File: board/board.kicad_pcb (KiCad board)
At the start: 2 copper layers, 102.4 x 54.4 mm, 20 parts, among them J1 FTDI_ISP, J2 ICSP, J3 Motor_Terminal, J4 Power, J5 Run, SW1 Run, SW2 Select, SW3 Up, SW4 Down, U1 ATmega328P-P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

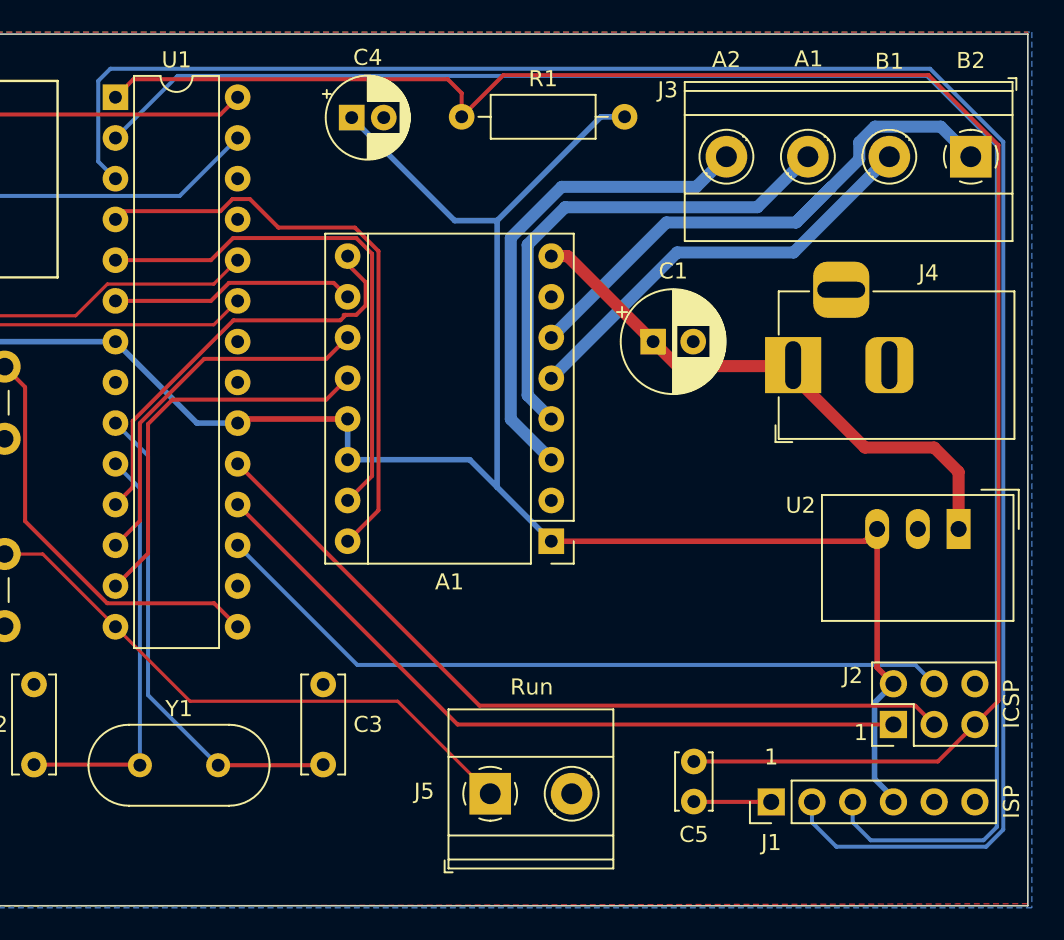
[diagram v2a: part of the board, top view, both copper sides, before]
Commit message: Fixed an overlapping trace that got missed in last DRC.
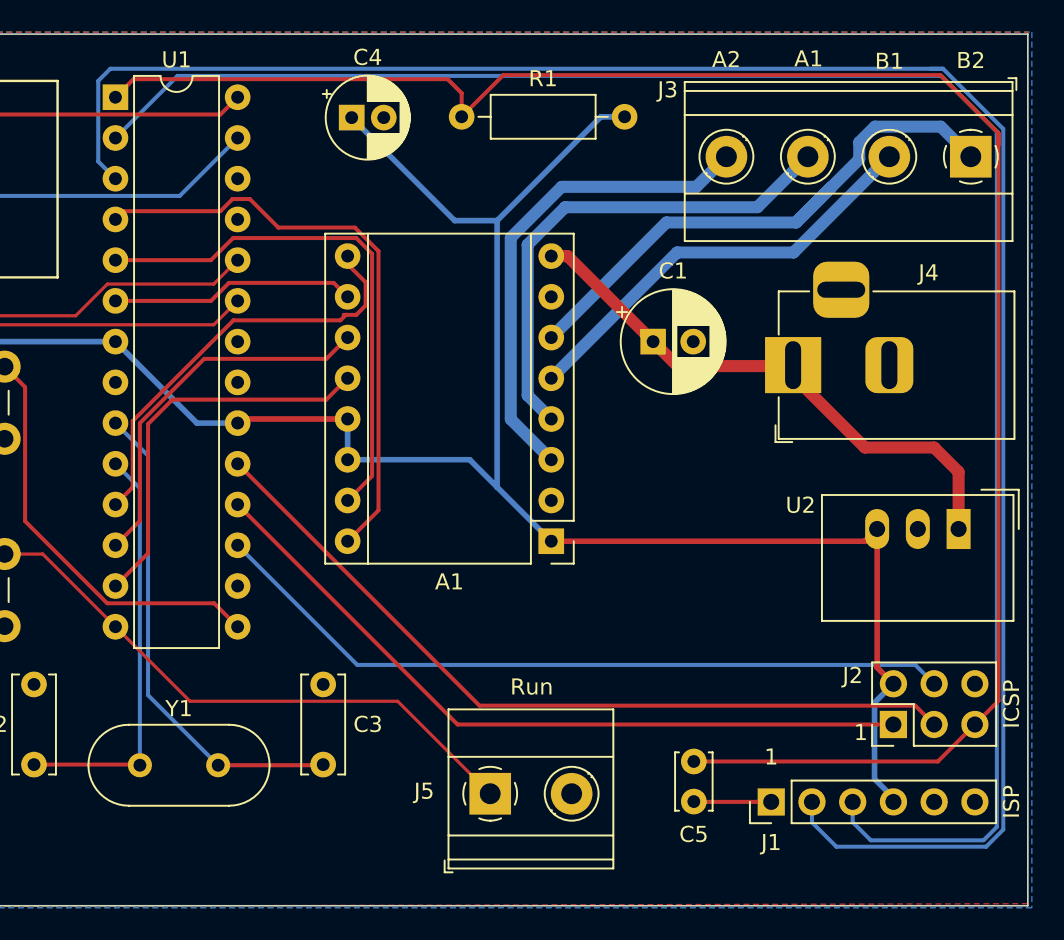
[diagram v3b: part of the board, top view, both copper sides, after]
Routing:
- net RX: track 111.9 -> 113.3 mm
- net TX: track 122.3 -> 123.6 mm
- net RESET: track 115.5 -> 116.6 mm
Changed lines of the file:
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@@
   (segment (start 175.514 72.336) (end 179.886 76.708) (width 0.25) (layer "B.Cu") (net 15))
   (segment (start 209.51 78.994) (end 214.376 78.994) (width 0.25) (layer "F.Cu") (net 16))
-  (segment (start 197.670211 33.672989) (end 195.072 36.2712) (width 0.25) (layer "F.Cu") (net 17))
-  (segment (start 224.186006 33.672989) (end 197.670211 33.672989) (width 0.25) (layer "F.Cu") (net 17))
-  (segment (start 227.076 74.168) (end 228.547011 72.696989) (width 0.25) (layer "F.Cu") (net 17))
+  (segment (start 224.919609 33.672989) (end 228.547011 37.300391) (width 0.25) (layer "F.Cu") (net 17))
+  (segment (start 228.547011 37.300391) (end 228.547011 38.033994) (width 0.25) (layer "F.Cu") (net 17))
+  (segment (start 195.072 36.2712) (end 197.670211 33.672989) (width 0.25) (layer "F.Cu") (net 17))
+  (segment (start 197.670211 33.672989) (end 224.919609 33.672989) (width 0.25) (layer "F.Cu") (net 17))
   (segment (start 194.200989 33.926989) (end 195.072 34.798) (width 0.25) (layer "F.Cu") (net 17))
+  (segment (start 228.547011 37.300391) (end 228.547011 72.696989) (width 0.25) (layer "F.Cu") (net 17))
+  (segment (start 228.547011 72.696989) (end 227.076 74.168) (width 0.25) (layer "F.Cu") (net 17))
   (segment (start 227.076 74.168) (end 224.77 76.474) (width 0.25) (layer "F.Cu") (net 17))
   (segment (start 195.072 34.798) (end 195.072 36.2712) (width 0.25) (layer "F.Cu") (net 17))
   (segment (start 224.77 76.474) (end 209.55 76.474) (width 0.25) (layer "F.Cu") (net 17))
   (segment (start 194.200989 33.926989) (end 174.607011 33.926989) (width 0.25) (layer "F.Cu") (net 17))
-  (segment (start 228.547011 72.696989) (end 228.547011 38.033994) (width 0.25) (layer "F.Cu") (net 17))
   (segment (start 174.607011 33.926989) (end 173.482 35.052) (width 0.25) (layer "F.Cu") (net 17))
-  (segment (start 228.547011 38.033994) (end 224.186006 33.672989) (width 0.25) (layer "F.Cu") (net 17))
-  (segment (start 228.447011 80.558006) (end 228.447011 38.081994) (width 0.25) (layer "B.Cu") (net 18))
-  (segment (start 220.581011 81.389011) (end 227.616006 81.389011) (width 0.25) (layer "B.Cu") (net 18))
-  (segment (start 177.351011 33.722989) (end 173.482 37.592) (width 0.25) (layer "B.Cu") (net 18))
-  (segment (start 219.456 78.994) (end 219.456 80.264) (width 0.25) (layer "B.Cu") (net 18))
-  (segment (start 228.447011 38.081994) (end 224.088006 33.722989) (width 0.25) (layer "B.Cu") (net 18))
-  (segment (start 227.616006 81.389011) (end 228.447011 80.558006) (width 0.25) (layer "B.Cu") (net 18))
-  (segment (start 224.088006 33.722989) (end 177.351011 33.722989) (width 0.25) (layer "B.Cu") (net 18))
-  (segment (start 219.456 80.264) (end 220.581011 81.389011) (width 0.25) (layer "B.Cu") (net 18))
-  (segment (start 228.847031 37.839031) (end 228.847031 80.7237) (width 0.25) (layer "B.Cu") (net 19))
-  (segment (start 227.7817 81.789031) (end 218.441031 81.789031) (width 0.25) (layer "B.Cu") (net 19))
-  (segment (start 218.441031 81.789031) (end 216.916 80.264) (width 0.25) (layer "B.Cu") (net 19))
-  (segment (start 172.406989 39.056989) (end 172.406989 34.031991) (width 0.25) (layer "B.Cu") (net 19))
-  (segment (start 173.16498 33.274) (end 224.282 33.274) (width 0.25) (layer "B.Cu") (net 19))
+  (segment (start 228.447011 37.200391) (end 228.447011 80.558006) (width 0.25) (layer "B.Cu") (net 18))
+  (segment (start 177.351011 33.722989) (end 224.969609 33.722989) (width 0.25) (layer "B.Cu") (net 18))
+  (segment (start 227.616006 81.389011) (end 220.581011 81.389011) (width 0.25) (layer "B.Cu") (net 18))
+  (segment (start 173.482 37.592) (end 177.351011 33.722989) (width 0.25) (layer "B.Cu") (net 18))
+  (segment (start 224.969609 33.722989) (end 228.447011 37.200391) (width 0.25) (layer "B.Cu") (net 18))
+  (segment (start 220.581011 81.389011) (end 219.456 80.264) (width 0.25) (layer "B.Cu") (net 18))
+  (segment (start 228.447011 37.200391) (end 228.447011 38.081994) (width 0.25) (layer "B.Cu") (net 18))
+  (segment (start 228.447011 80.558006) (end 227.616006 81.389011) (width 0.25) (layer "B.Cu") (net 18))
+  (segment (start 219.456 80.264) (end 219.456 78.994) (width 0.25) (layer "B.Cu") (net 18))
+  (segment (start 216.916 80.264) (end 218.441031 81.789031) (width 0.25) (layer "B.Cu") (net 19))
+  (segment (start 228.847031 80.7237) (end 228.847031 37.034697) (width 0.25) (layer "B.Cu") (net 19))
+  (segment (start 218.441031 81.789031) (end 227.7817 81.789031) (width 0.25) (layer "B.Cu") (net 19))
+  (segment (start 228.847031 37.034697) (end 225.086334 33.274) (width 0.25) (layer "B.Cu") (net 19))
   (segment (start 216.916 78.994) (end 216.916 80.264) (width 0.25) (layer "B.Cu") (net 19))
-  (segment (start 173.482 40.132) (end 172.406989 39.056989) (width 0.25) (layer "B.Cu") (net 19))
-  (segment (start 228.847031 80.7237) (end 227.7817 81.789031) (width 0.25) (layer "B.Cu") (net 19))
-  (segment (start 224.282 33.274) (end 228.847031 37.839031) (width 0.25) (layer "B.Cu") (net 19))
-  (segment (start 172.406989 34.031991) (end 173.16498 33.274) (width 0.25) (layer "B.Cu") (net 19))
+  (segment (start 172.406989 34.031991) (end 172.406989 39.056989) (width 0.25) (layer "B.Cu") (net 19))
+  (segment (start 225.086334 33.274) (end 173.16498 33.274) (width 0.25) (layer "B.Cu") (net 19))
+  (segment (start 172.406989 39.056989) (end 173.482 40.132) (width 0.25) (layer "B.Cu") (net 19))
+  (segment (start 227.7817 81.789031) (end 228.847031 80.7237) (width 0.25) (layer "B.Cu") (net 19))
+  (segment (start 225.086334 33.274) (end 224.282 33.274) (width 0.25) (layer "B.Cu") (net 19))
+  (segment (start 173.16498 33.274) (end 172.406989 34.031991) (width 0.25) (layer "B.Cu") (net 19))
   (segment (start 223.360989 70.452989) (end 188.562989 70.452989) (width 0.25) (layer "B.Cu") (net 20))
   (segment (start 224.536 71.628) (end 223.360989 70.452989) (width 0.25) (layer "B.Cu") (net 20))

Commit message: Fixed incorrect +5v to GND connection.
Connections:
- A1 pad 1: +5V -> GND
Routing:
- net +5V: track 156.0 -> 174.0 mm
- net +24V: track 35.2 -> 36.3 mm
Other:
- board text added: "Rev: A"
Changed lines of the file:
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@@
     (fp_line (start 13.97 -1.27) (end 13.97 19.05) (layer "F.Fab") (width 0.1))
     (pad "1" thru_hole rect (at 0 0 180) (locked) (size 1.6 1.6) (drill 0.8) (layers *.Cu *.Mask)
-      (net 5 "+5V") (pinfunction "GND") (pintype "power_in"))
+      (net 4 "GND") (pinfunction "GND") (pintype "power_in"))
     (pad "2" thru_hole oval (at 0 2.54 180) (locked) (size 1.6 1.6) (drill 0.8) (layers *.Cu *.Mask)
       (net 8 "unconnected-(A1-Pad2)") (pinfunction "~FLT") (pintype "output+no_connect"))
@@
     (fp_circle (center 3.25 2.25) (end 1.25 2.5) (layer "F.Fab") (width 0.1) (fill none))
     (pad "1" thru_hole circle (at 0 0 90) (locked) (size 2 2) (drill 1.1) (layers *.Cu *.Mask)
-      (net 23 "BTN_RUN") (pinfunction "1"))
+      (net 23 "BTN_RUN") (pinfunction "1") (pintype "passive"))
     (pad "1" thru_hole circle (at 6.5 0 90) (locked) (size 2 2) (drill 1.1) (layers *.Cu *.Mask)
-      (net 23 "BTN_RUN") (pinfunction "1"))
+      (net 23 "BTN_RUN") (pinfunction "1") (pintype "passive"))
     (pad "2" thru_hole circle (at 6.5 4.5 90) (locked) (size 2 2) (drill 1.1) (layers *.Cu *.Mask)
-      (net 4 "GND") (pinfunction "2"))
+      (net 4 "GND") (pinfunction "2") (pintype "passive"))
     (pad "2" thru_hole circle (at 0 4.5 90) (locked) (size 2 2) (drill 1.1) (layers *.Cu *.Mask)
-      (net 4 "GND") (pinfunction "2"))
+      (net 4 "GND") (pinfunction "2") (pintype "passive"))
     (model "${KICAD6_3DMODEL_DIR}/Button_Switch_THT.3dshapes/SW_PUSH_6mm_H5mm.wrl"
       (offset (xyz 0 0 0))
@@
     (effects (font (size 1 1) (thickness 0.15)))
   )
+  (gr_text "Rev: A" (at 132.1308 82.9564) (layer "F.SilkS")
+    (effects (font (size 1 1) (thickness 0.15)))
+  )
   (segment (start 189.885051 44.65232) (end 189.885051 60.812949) (width 0.25) (layer "F.Cu") (net 1))
   (segment (start 173.482 42.672) (end 173.998006 42.155994) (width 0.25) (layer "F.Cu") (net 1))
@@
   (segment (start 215.887493 51.7575) (end 215.742 51.7575) (width 0.75) (layer "F.Cu") (net 2))
   (segment (start 201.676 44.958) (end 200.66 44.958) (width 0.75) (layer "F.Cu") (net 2))
-  (segment (start 208.535011 51.817011) (end 207.01 50.292) (width 0.75) (layer "F.Cu") (net 2))
-  (segment (start 215.682489 51.817011) (end 208.535011 51.817011) (width 0.75) (layer "F.Cu") (net 2))
   (segment (start 226.06 61.976) (end 226.06 61.930007) (width 0.75) (layer "F.Cu") (net 2))
   (segment (start 220.218 56.896) (end 215.742 52.42) (width 0.75) (layer "F.Cu") (net 2))
@@
   (segment (start 207.01 50.292) (end 201.676 44.958) (width 0.75) (layer "F.Cu") (net 2))
   (segment (start 224.536 56.896) (end 220.218 56.896) (width 0.75) (layer "F.Cu") (net 2))
+  (segment (start 212.901489 48.916989) (end 215.742 51.7575) (width 0.75) (layer "B.Cu") (net 2))
+  (segment (start 208.385011 48.916989) (end 212.901489 48.916989) (width 0.75) (layer "B.Cu") (net 2))
+  (segment (start 207.01 50.292) (end 208.385011 48.916989) (width 0.75) (layer "B.Cu") (net 2))
   (segment (start 180.815994 43.832989) (end 188.500006 43.832989) (width 0.25) (layer "F.Cu") (net 3))
   (segment (start 189.485031 58.672969) (end 189.485031 44.818014) (width 0.25) (layer "F.Cu") (net 3))
@@
   (segment (start 189.485031 44.818014) (end 188.500006 43.832989) (width 0.25) (layer "F.Cu") (net 3))
   (segment (start 220.98 61.976) (end 220.98 70.612) (width 0.35) (layer "F.Cu") (net 5))
+  (segment (start 223.6724 64.6684) (end 226.568 64.6684) (width 0.35) (layer "F.Cu") (net 5))
+  (segment (start 220.98 61.976) (end 223.6724 64.6684) (width 0.35) (layer "F.Cu") (net 5))
   (segment (start 181.356 55.118) (end 181.102 55.372) (width 0.35) (layer "F.Cu") (net 5))
-  (segment (start 200.66 62.738) (end 220.218 62.738) (width 0.35) (layer "F.Cu") (net 5))
+  (segment (start 227.838 63.3984) (end 227.838 47.6504) (width 0.35) (layer "F.Cu") (net 5))
+  (segment (start 227.838 47.6504) (end 222.1484 41.9608) (width 0.35) (layer "F.Cu") (net 5))
+  (segment (start 205.232 40.132) (end 205.232 36.2712) (width 0.35) (layer "F.Cu") (net 5))
   (segment (start 220.98 70.612) (end 221.996 71.628) (width 0.35) (layer "F.Cu") (net 5))
-  (segment (start 220.218 62.738) (end 220.98 61.976) (width 0.35) (layer "F.Cu") (net 5))
+  (segment (start 222.1484 41.9608) (end 207.0608 41.9608) (width 0.35) (layer "F.Cu") (net 5))
+  (segment (start 207.0608 41.9608) (end 205.232 40.132) (width 0.35) (layer "F.Cu") (net 5))
   (segment (start 187.96 55.118) (end 181.356 55.118) (width 0.35) (layer "F.Cu") (net 5))
+  (segment (start 226.568 64.6684) (end 227.838 63.3984) (width 0.35) (layer "F.Cu") (net 5))
   (segment (start 173.482 50.292) (end 142.494 50.292) (width 0.35) (layer "B.Cu") (net 5))
   (segment (start 205.232 36.2712) (end 203.7588 36.2712) (width 0.35) (layer "B.Cu") (net 5))
@@
   (segment (start 178.562 55.372) (end 173.482 50.292) (width 0.35) (layer "B.Cu") (net 5))
   (segment (start 181.356 55.118) (end 181.102 55.372) (width 0.35) (layer "B.Cu") (net 5))
-  (segment (start 200.66 62.738) (end 197.284949 59.362949) (width 0.35) (layer "B.Cu") (net 5))
-  (segment (start 187.96 57.658) (end 195.58 57.658) (width 0.35) (layer "B.Cu") (net 5))
+  (segment (start 187.96 55.118) (end 197.284949 45.793051) (width 0.35) (layer "B.Cu") (net 5))
   (segment (start 181.102 55.372) (end 178.562 55.372) (width 0.35) (layer "B.Cu") (net 5))
   (segment (start 220.820989 77.564989) (end 221.996 78.74) (width 0.35) (layer "B.Cu") (net 5))
   (segment (start 220.820989 72.803011) (end 220.820989 77.564989) (width 0.35) (layer "B.Cu") (net 5))
+  (segment (start 197.284949 45.793051) (end 197.284949 42.745051) (width 0.35) (layer "B.Cu") (net 5))
   (segment (start 194.637051 42.745051) (end 197.284949 42.745051) (width 0.35) (layer "B.Cu") (net 5))
   (segment (start 203.7588 36.2712) (end 197.284949 42.745051) (width 0.35) (layer "B.Cu") (net 5))
-  (segment (start 197.284949 59.362949) (end 197.284949 42.745051) (width 0.35) (layer "B.Cu") (net 5))
   (segment (start 221.996 78.74) (end 221.996 78.994) (width 0.35) (layer "B.Cu") (net 5))
-  (segment (start 195.58 57.658) (end 197.284949 59.362949) (width 0.35) (layer "B.Cu") (net 5))
   (segment (start 221.996 71.628) (end 220.820989 72.803011) (width 0.35) (layer "B.Cu") (net 5))
   (segment (start 188.214 36.322) (end 194.637051 42.745051) (width 0.35) (layer "B.Cu") (net 5))
